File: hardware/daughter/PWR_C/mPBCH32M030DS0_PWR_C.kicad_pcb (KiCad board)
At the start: 2 copper layers, 60 x 42 mm, 75 parts, among them J1 B2B_PWR, J2 OUT0, J3 B2B_SIG, J4 OUT1, J5 OUT2, J6 OUT3, Q1 MTN2306AN3, Q2 MTN2306AN3, Q3 MTN2306AN3, Q4 MTN2306AN3, Q5 MTN2306AN3, Q6 MTN2306AN3, Q7 MTN2306AN3, Q8 MTN2306AN3

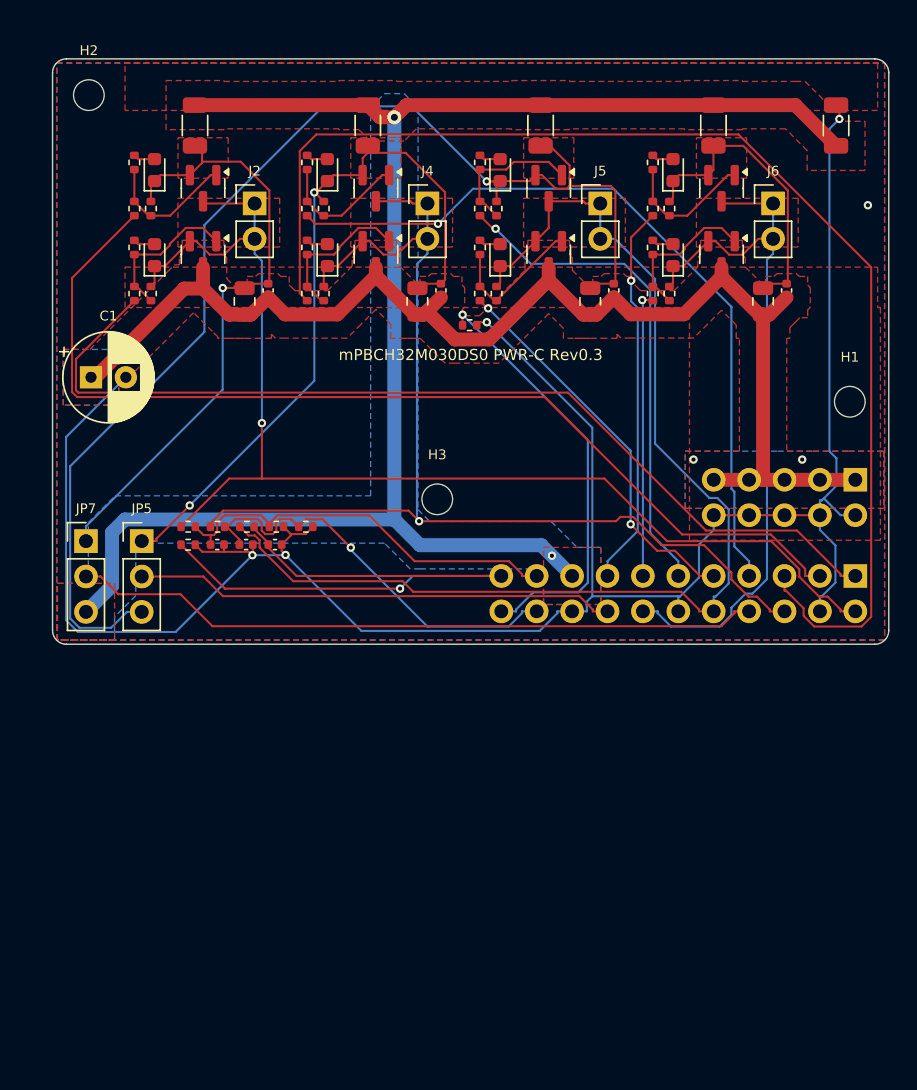
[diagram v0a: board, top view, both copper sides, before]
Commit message: Rev 0.4: DIP-42 MCU module + power boards A/B/C (KiCad 8)
- MCU module: 20.32 x 53.34mm (8 x 21 grid), DIP-42 (0.6in rows), fits
  an 82 x 52mm breadboard. Headers can be fitted from either side;
  signal names on bottom silk. All LEDs (power, status, 8 gate LEDs) on
  the module top.
- Power boards take the module in two 1x21 sockets (left/right
  symmetric mating). FETs/shunts on the heatsink side, no LEDs.
  Voltage-dependent parts (TVS, OVP divider, bulk caps, BEMF divider)
  moved to the power boards. Breakout board D removed.
  A/C: 20.32 x 71.94mm, B (TO-263 x8): 40.64 x 66.94mm.
- Capacitors re-selected for realistic size vs voltage/capacitance
  (4.7uF 1608, 10uF/25V 2012, 10uF/50V 1206, 4.7nF/100V 1608, low
  profile electrolytics).
- Schematics and boards generated in KiCad 8 format; netlists verified
  with KiCad 8.0.9.
- Layout pipeline: Freerouting bridge (parallel), second pass, early
  repair before pours, island-aware maze repair, DRC via kicad-cli.
- DRC: power boards A/B/C have 0 unconnected / 0 electrical errors.
  The MCU module still has unrouted connections (work in progress).

Co-Authored-By: Claude Opus 5.5 <noreply@anthropic.com>
Claude-Session: https://claude.ai/code/session_01LENFjjhDfYjJZV1NWhB9uV
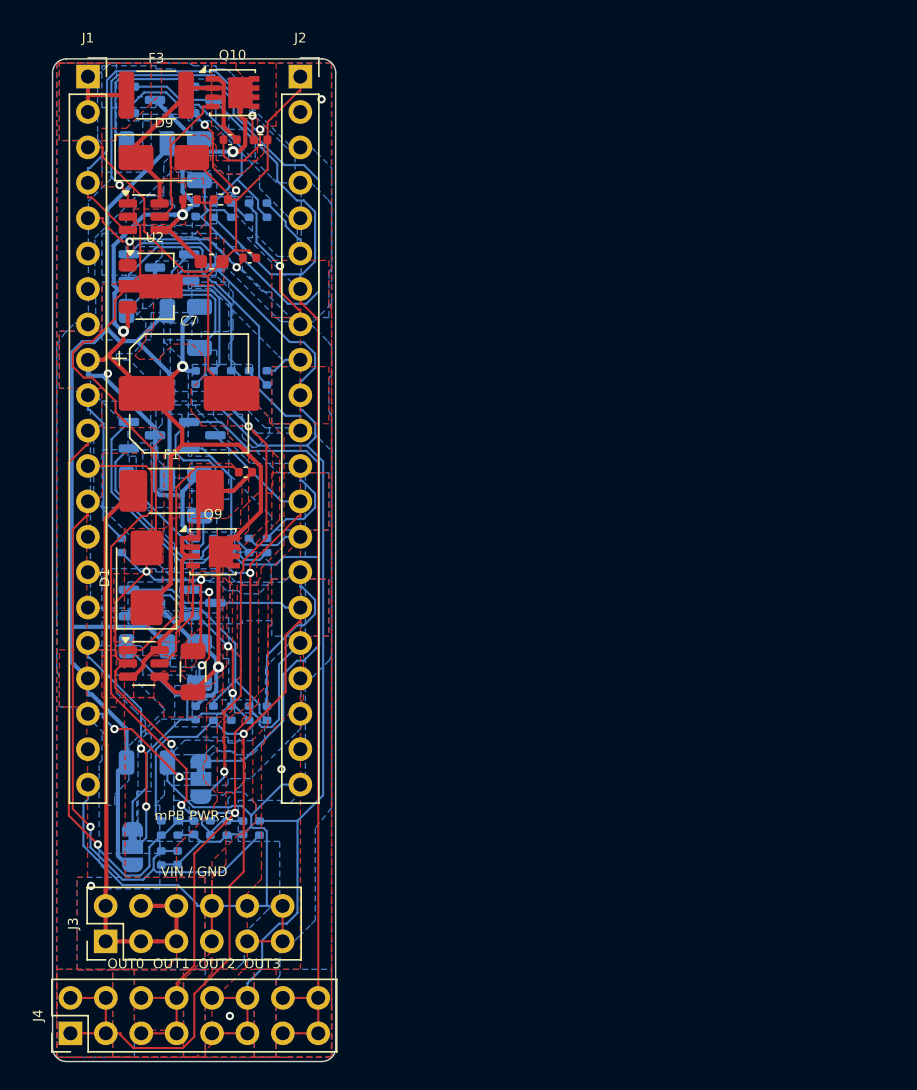
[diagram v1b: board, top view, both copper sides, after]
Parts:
- removed D10: RED GH0, LED_0603_1608Metric
- removed D11: GREEN GL0, LED_0603_1608Metric
- removed D12: RED GH1, LED_0603_1608Metric
- removed D13: GREEN GL1, LED_0603_1608Metric
- removed D14: RED GH2, LED_0603_1608Metric
- removed D15: GREEN GL2, LED_0603_1608Metric
- removed D16: RED GH3, LED_0603_1608Metric
- removed D17: GREEN GL3, LED_0603_1608Metric
- removed H1, H2, H3: M2, MountingHole_2.2mm_M2
- removed J5: OUT2, PinHeader_1x02_P2.54mm_Vertical
- removed J6: OUT3, PinHeader_1x02_P2.54mm_Vertical
- removed R35, R36, R45, R46, R55, R56, R65, R66: 22k, R_0402_1005Metric
- added C3: 1uF/50V, C_0603_1608Metric, F.Cu at (11.4, 14.5)
- added C4: 1uF/25V, C_0402_1005Metric, F.Cu at (14.1, 14.3)
- added C5: 0.1uF/50V, C_0402_1005Metric, F.Cu at (13.8, 29.7)
- added C6: 0.1uF/50V, C_0402_1005Metric, F.Cu at (12.7, 5.79)
- added C7: 100uF/25V, CP_Elec_8x6.2, F.Cu at (9.79, 24.0)
- added D1: SMBJ16A, D_SMB, F.Cu at (6.75, 37.2)
- added D9: SMAJ20A, D_SMA, F.Cu at (8.00, 7.08)
- added F1: 10A, Fuse_Littelfuse_NANO2_2410, F.Cu at (8.54, 31.0)
- added F3: 5A, Fuse_1812_4532Metric, F.Cu at (7.45, 2.60)
- added Q10: TPN1R603PL, Vishay_PowerPAK_1212-8_Single, F.Cu at (12.9, 2.42)
- added Q9: TPN2R304PL, Vishay_PowerPAK_1212-8_Single, F.Cu at (11.5, 35.4)
- added R11: 110k 1%, R_0402_1005Metric, F.Cu at (9.87, 10.1)
- added R12: 10k 1%, R_0402_1005Metric, F.Cu at (12.1, 10.1)
- added R6: 100k, R_0402_1005Metric, F.Cu at (14.9, 5.80)
- added U2: 78L05, SOT-89-3, F.Cu at (7.34, 16.3)
- added U4: LM74700-Q1, SOT-23-6, F.Cu at (6.54, 43.4)
- added U5: LM74700-Q1, SOT-23-6, F.Cu at (6.54, 11.3)
- C1: value 220uF/25V -> 10uF/50V; footprint CP_Radial_D6.3mm_P2.50mm -> C_1206_3216Metric
- C30, C40, C50, C60, C71, C72, C73, Q1, Q2, Q3, Q4, Q5, Q6, Q7, Q8, R30, R31, R32, R33, R34, R40, R41, R42, R43, R44, R50, R51, R52, R53, R54, R60, R61, R62, R63, R64, R70, R71, R72, R74, R75, R77, R78, TH1: moved to B.Cu
- C31, C41, C51, C61: footprint C_0805_2012Metric -> C_1206_3216Metric; moved to B.Cu
- J1: value B2B_PWR -> SOCK_L; footprint PinSocket_2x05_P2.54mm_Vertical -> PinSocket_1x21_P2.54mm_Vertical; moved to F.Cu
- J2: value OUT0 -> SOCK_R; footprint PinHeader_1x02_P2.54mm_Vertical -> PinSocket_1x21_P2.54mm_Vertical
- J3: value B2B_SIG -> PWR_IN; footprint PinSocket_2x11_P2.54mm_Vertical -> PinHeader_2x06_P2.54mm_Vertical; moved to F.Cu
- J4: value OUT1 -> MOTOR; footprint PinHeader_1x02_P2.54mm_Vertical -> PinHeader_2x08_P2.54mm_Vertical
- JP5, JP7: footprint PinHeader_1x03_P2.54mm_Vertical -> SolderJumper-3_P1.3mm_Bridged12_RoundedPad1.0x1.5mm_NumberLabels; moved to B.Cu
- moved R70 67.3 mm to (6.78, 50.5), turned to 0 degrees
- moved J4 64.8 mm to (1.28, 69.9), turned to 90 degrees
- moved J1 62.2 mm to (2.54, 1.27), turned to 0 degrees
- moved J3 59.8 mm to (3.81, 63.3)
- moved Q7 43.0 mm to (6.42, 2.94), turned to 0 degrees
- moved C60 42.8 mm to (10.3, 10.8), turned to -90 degrees
- moved C61 41.7 mm to (10.5, 7.24), turned to -90 degrees
- moved R64 40.7 mm to (6.78, 6.05), turned to 0 degrees
- moved Q8 37.8 mm to (10.7, 2.94), turned to 0 degrees
- moved R34 37.5 mm to (6.78, 42.1), turned to 0 degrees
- moved R32 37.1 mm to (14.1, 46.9), turned to -90 degrees
- moved R33 36.7 mm to (12.8, 46.9), turned to -90 degrees
- moved R61 33.3 mm to (11.5, 10.9), turned to -90 degrees
- moved R30 31.6 mm to (15.4, 46.9), turned to -90 degrees
- moved R63 31.4 mm to (12.8, 10.9), turned to -90 degrees
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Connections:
- J1 pad 1: VBUS -> USB_VBUS
- J1 pad 10: GND -> NTC
- J1 pad 2: GND -> USB_VBUS
- J1 pad 3: VBUS -> VBUS_SNS
- J1 pad 4: GND -> PD_PWR_EN
- J1 pad 5: VBUS -> +5V
- J1 pad 6: GND -> +3V3
- J1 pad 7: VBUS -> SWDIO
- J1 pad 8: GND -> nRST
- J2 pad 1: SW0 -> GND
- J2 pad 2: SW0 -> UART_TX
- J3 pad 1: HO0 -> VIN
- J3 pad 10: SW2 -> GND
- J3 pad 11: LO2 -> GND
- J3 pad 2: SW0 -> VIN
- J3 pad 3: LO0 -> VIN
- J3 pad 4: GND -> VIN
- J3 pad 5: HO1 -> VIN
- J3 pad 6: SW1 -> VIN
- J3 pad 7: LO1 -> GND
- J3 pad 8: ISA_SEL -> GND
- J3 pad 9: HO2 -> GND
- J4 pad 1: SW1 -> SW0
- J4 pad 2: SW1 -> SW0
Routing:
- net HO1: track 90.4 -> 7.86 mm
- net LO0: track 73.9 -> 9.47 mm
- net HO0: track 69.7 -> 11.8 mm
- net LO1: track 55.1 -> 4.12 mm, vias 1 -> 0
- net VIN: track 0.00 -> 43.3 mm, vias 0 -> 1
- net VBUS: track 91.4 -> 134.6 mm, vias 2 -> 6
- net SW3: track 52.4 -> 91.0 mm
- net ISH: track 118.3 -> 81.7 mm, vias 2 -> 0
- net SRC2: track 88.3 -> 52.3 mm, vias 1 -> 2
- net ISA_SEL: track 49.6 -> 17.0 mm, vias 0 -> 2
- net LO2: track 35.8 -> 6.44 mm, vias 1 -> 0
- net VCAP2: track 0.00 -> 27.7 mm, vias 0 -> 2
- net PD_PWR_EN: track 0.00 -> 27.0 mm, vias 0 -> 1
- net SRC3: track 21.7 -> 47.7 mm
- net HO2: track 28.1 -> 2.72 mm, vias 2 -> 0
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- added copper zone on B.Cu, net SRC0
- added copper zone on B.Cu, net SRC1
- added copper zone on B.Cu, net SRC2
- added copper zone on B.Cu, net SRC3
- added copper zone on B.Cu, net SW0
- added copper zone on B.Cu, net SW1
- added copper zone on B.Cu, net SW2
- added copper zone on B.Cu, net SW3
- added copper zone on B.Cu, net USB_VBUS
- added copper zone on F.Cu, net USB_VBUS
- added copper zone on F.Cu, net USB_VBUS_P
- added copper zone on B.Cu, net VIN
- added copper zone on F.Cu, net VIN
- added copper zone on F.Cu, net VIN_F
- removed copper zone on F.Cu, net SRC1
- removed copper zone on F.Cu, net SRC3
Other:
- board size 60 x 42 mm -> 20.3 x 71.9 mm
- board text added: "OUT0 OUT1 OUT2 OUT3"
- board text added: "VIN / GND"
- board text added: "mPB PWR-C"
- board text removed: "mPBCH32M030DS0 PWR-C Rev0.3"

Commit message: Rev 0.4: rework module pinout for routability, power boards regenerated
- Module edge pin order follows the CH32M030 QFN48 pin sides so the
  breakout traces nest instead of crossing (J1: USB_VBUS, PD_PWR_EN,
  PC4/PC5, +3V3, +5V, SWDIO, VBUS, NTC, BEMF, HALL, ISx, TACH;
  J2: RX/TX, nRST, gate drive HO3..LO0, VBUS_SNS, I2C, nFAULT).
- Module: area under the QFN kept for fan-out (filters and the VHV/USB
  diode block moved away, gate LEDs right-aligned to J2).
- Power boards A/B/C re-placed for the new pinout (VBUS divider next to
  J2 VBUS_SNS, LM74700 next to its FET) and re-routed: all three at
  0 unconnected / 0 electrical DRC errors.
- Layout tooling: DRC via kicad-cli in a separate process, reload after
  SES import, selectable Freerouting jar, optional rip-up repair,
  configurable Freerouting timeout.
- MCU module still has unrouted connections (work in progress).

Co-Authored-By: Claude Opus 5.5 <noreply@anthropic.com>
Claude-Session: https://claude.ai/code/session_01LENFjjhDfYjJZV1NWhB9uV
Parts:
- moved C71 32.4 mm to (7.31, 22.9)
- moved R71 32.4 mm to (4.96, 22.9)
- moved R72 32.4 mm to (6.14, 22.9)
- moved C72 20.9 mm to (8.49, 34.9)
- moved R75 20.9 mm to (7.32, 34.9)
- moved R74 20.9 mm to (6.14, 34.9)
- moved R11 20.1 mm to (5.42, 29.7)
- moved R12 20.1 mm to (7.62, 29.7)
- moved R77 12.9 mm to (4.96, 46.9)
- moved C73 10.5 mm to (7.31, 46.9)
- moved R78 10.5 mm to (6.14, 46.9)
- moved C3 4.31 mm to (10.4, 10.4)
- moved C4 4.31 mm to (13.1, 10.1)
- moved C1 1.73 mm to (10.1, 45.7)
- moved D1 1.73 mm to (6.75, 39.0)
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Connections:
- J1 pad 3: VBUS_SNS -> PD_PWR_EN
- J1 pad 4: PD_PWR_EN -> GPIO_PC4
- J1 pad 5: +5V -> GPIO_PC5
- J1 pad 7: SWDIO -> +5V
- J1 pad 8: nRST -> SWDIO
- J2 pad 10: SW2 -> LO2
- J2 pad 11: LO2 -> HO1
- J2 pad 12: HO1 -> SW1
- J2 pad 13: SW1 -> LO1
- J2 pad 14: LO1 -> HO0
- J2 pad 15: HO0 -> SW0
- J2 pad 16: SW0 -> LO0
- J2 pad 17: LO0 -> VBUS_SNS
- J2 pad 18: I2C_SDA -> I2C_SCL
- J2 pad 19: I2C_SCL -> I2C_SDA
- J2 pad 2: UART_TX -> UART_RX
- J2 pad 3: UART_RX -> UART_TX
- J2 pad 4: GPIO_PC4 -> nRST
- J2 pad 5: GPIO_PC5 -> HO3
- J2 pad 6: HO3 -> SW3
- J2 pad 7: SW3 -> LO3
- J2 pad 8: LO3 -> HO2
- J2 pad 9: HO2 -> SW2
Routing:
- net GND: track 156.2 -> 206.4 mm, vias 5 -> 9
- net SW0: track 74.5 -> 123.0 mm
- net BEMF_U: track 41.6 -> 7.18 mm, vias 1 -> 0
- net SRC3: track 47.7 -> 20.2 mm
- net BEMF_V: track 38.6 -> 11.2 mm, vias 1 -> 0
- net SW2: track 87.5 -> 111.2 mm, vias 1 -> 0
- net VBUS: track 134.6 -> 119.0 mm, vias 6 -> 4
- net VCAP2: track 27.7 -> 13.4 mm
- net VBUS_SNS: track 20.4 -> 34.5 mm
- net SRC0: track 30.4 -> 42.7 mm, vias 2 -> 0
- net SRC1: track 64.4 -> 53.7 mm, vias 0 -> 4
- net GH2: track 29.9 -> 21.6 mm
- net SRC2: track 52.3 -> 59.8 mm, vias 2 -> 0
- net GH0: track 18.8 -> 25.6 mm
- net VCAP1: track 19.0 -> 25.6 mm
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- added copper zone on F.Cu, net SRC1
- removed copper zone on F.Cu, net SRC0
- removed copper zone on F.Cu, net SRC2

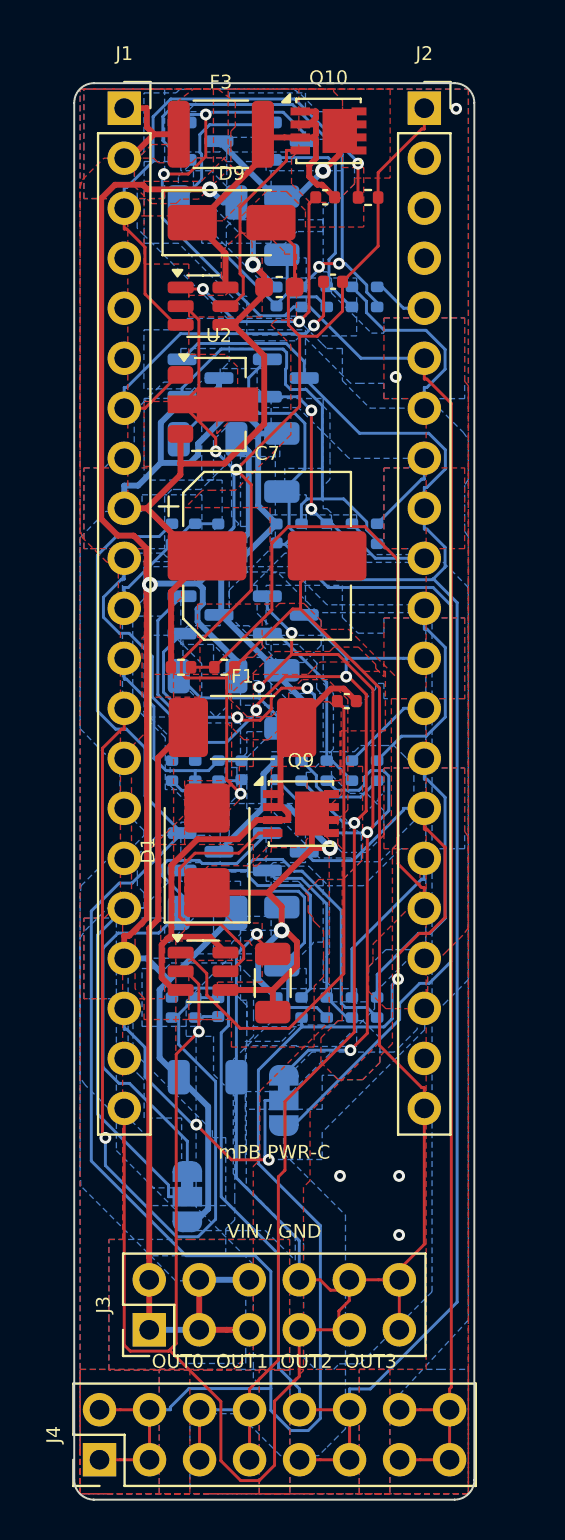
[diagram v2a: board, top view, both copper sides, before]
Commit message: 9マス版に一本化 (8マス版を削除)
- 8 マス版 (20.32mm) は JLCPCB の 2 層標準 0.127mm で配線しきれないため削除
- 9 マス版 (22.86mm, 端子列 0.7in) を hardware/ 直下・hardware/daughter/・hardware/fab/・docs/pcb/ へ移動
- ベタなし版は hardware/nopour/ (図は docs/pcb/nopour/)
- gen_pcb.py から MPB_W9 の切り替えを外し 9 マス固定に。既定ルールは 0.127mm / ビア 0.6/0.3
  (再生成した配置が確定済みの 4 基板と一致することを確認)
- 回路図の注記 (外形・列間) を 22.86mm / 17.78mm に更新し PDF を再出力
- README / stacking.md / design.md を 9 マス版のみの記述に更新

Co-Authored-By: Claude Opus 5.5 <noreply@anthropic.com>
Claude-Session: https://claude.ai/code/session_01LENFjjhDfYjJZV1NWhB9uV
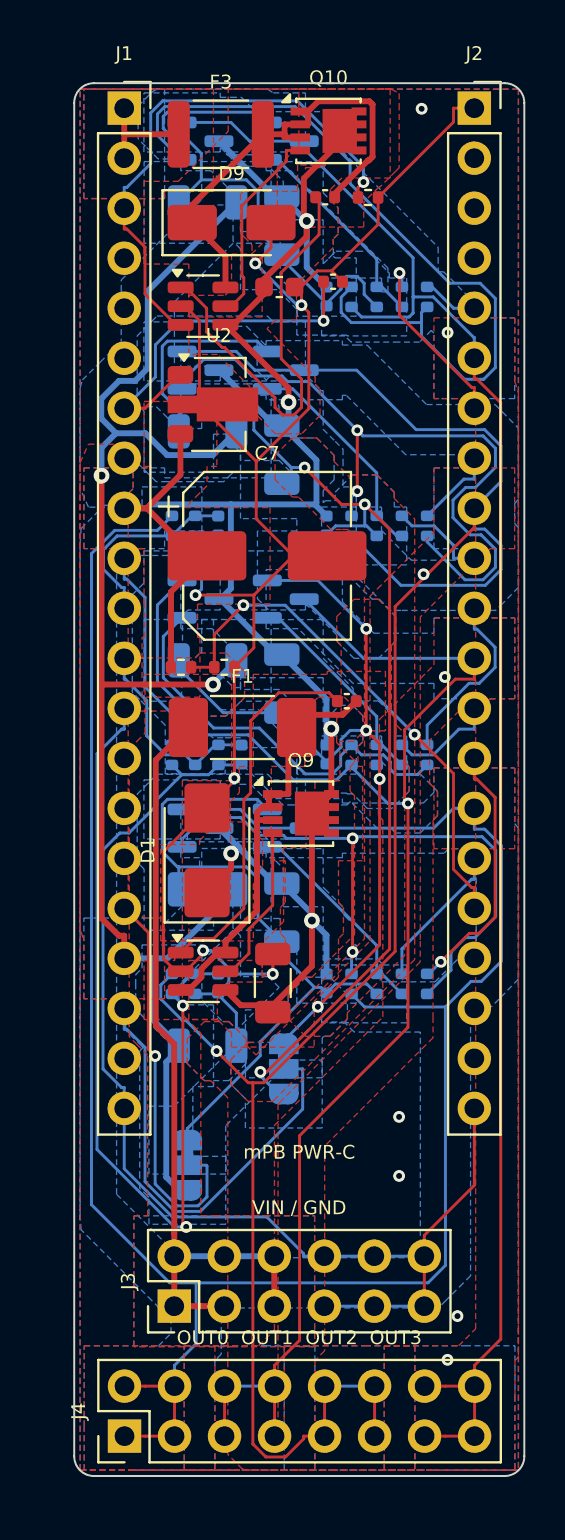
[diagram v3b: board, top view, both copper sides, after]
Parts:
- moved R30 2.81 mm to (17.9, 45.7)
- moved R31 2.81 mm to (14.1, 45.7)
- moved R33 2.81 mm to (15.4, 45.7)
- moved C30 2.81 mm to (12.8, 45.7)
- moved R32 2.81 mm to (16.6, 45.7)
- moved R40 2.66 mm to (17.9, 34.1)
- moved R41 2.66 mm to (14.1, 34.1)
- moved R43 2.66 mm to (15.4, 34.1)
- moved R42 2.66 mm to (16.6, 34.1)
- moved C40 2.66 mm to (12.8, 34.1)
- moved R50 2.57 mm to (17.9, 22.5)
- moved R51 2.57 mm to (14.1, 22.5)
- moved R53 2.57 mm to (15.4, 22.5)
- moved R52 2.57 mm to (16.6, 22.5)
- moved C50 2.57 mm to (12.8, 22.5)
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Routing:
- net GND: track 206.4 -> 152.8 mm, vias 9 -> 10
- net GH3: track 24.2 -> 40.7 mm, vias 2 -> 0
- net GH2: track 21.6 -> 36.4 mm, vias 0 -> 2
- net SRC1: track 53.7 -> 43.2 mm
- net ISH: track 86.9 -> 77.9 mm
- net VCAP2: track 13.4 -> 21.9 mm, vias 2 -> 0
- net VBUS: track 119.0 -> 110.9 mm, vias 4 -> 5
- net VBUS_SNS: track 34.5 -> 26.5 mm, vias 0 -> 2
- net GH0: track 25.6 -> 33.4 mm, vias 0 -> 2
- net SRC0: track 42.7 -> 35.4 mm
- net ISB_SEL: track 16.1 -> 23.1 mm, vias 2 -> 0
- net VCAP1: track 25.6 -> 19.0 mm
- net SRC3: track 20.2 -> 26.3 mm
- net VIN_F: track 27.5 -> 21.5 mm
- net SW0: track 123.0 -> 117.5 mm, vias 1 -> 0
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- added copper zone on F.Cu, net SRC2
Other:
- board size 20.3 x 71.9 mm -> 22.9 x 70.7 mm
